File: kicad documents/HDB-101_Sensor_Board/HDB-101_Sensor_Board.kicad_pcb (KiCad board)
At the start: 2 copper layers, 90 x 18 mm, 4 parts, among them J1 Chassis sensor cable

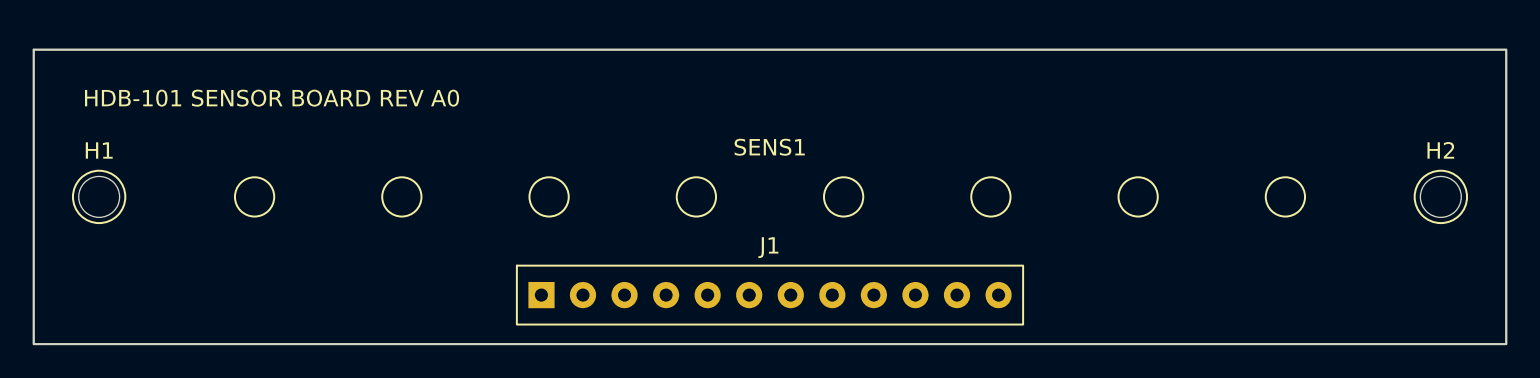
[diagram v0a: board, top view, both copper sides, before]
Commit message: Advance Rev A0 cockpit firmware and PCB bring-up
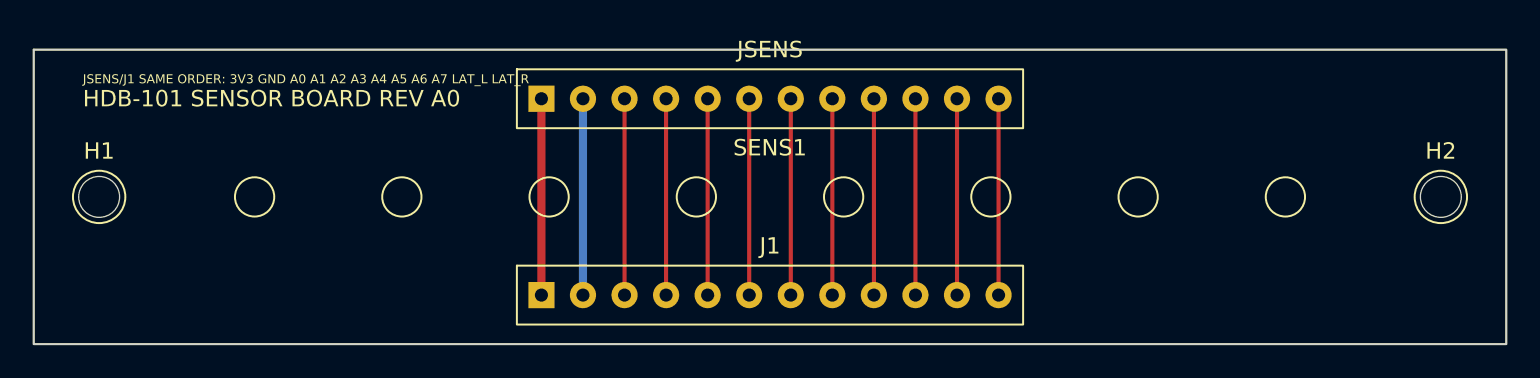
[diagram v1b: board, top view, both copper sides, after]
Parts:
- added JSENS: Sensor module header HPS order, PEGASUS_Placeholders:PinHeader_1x12_2p54, F.Cu at (45.0, 3.00)
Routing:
- net LAT_R: track 0.00 -> 12.0 mm
- net LAT_L: track 0.00 -> 12.0 mm
- net GND: track 0.00 -> 12.0 mm
- net A7: track 0.00 -> 12.0 mm
- net A6: track 0.00 -> 12.0 mm
- net A5: track 0.00 -> 12.0 mm
- net A4: track 0.00 -> 12.0 mm
- net A3: track 0.00 -> 12.0 mm
- net A2: track 0.00 -> 12.0 mm
- net A1: track 0.00 -> 12.0 mm
- net A0: track 0.00 -> 12.0 mm
- net 3V3: track 0.00 -> 12.0 mm
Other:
- board text added: "JSENS/J1 SAME ORDER: 3V3 GND A0 A1 A2 A3 A4 A5 A6 A7 LAT_L LAT_R"
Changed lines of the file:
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@@
     (effects (font (size 0.8 0.8) (thickness 0.15)) (justify left))
+  )
+  (gr_text "JSENS/J1 SAME ORDER: 3V3 GND A0 A1 A2 A3 A4 A5 A6 A7 LAT_L LAT_R" (at 3 1.8) (layer "F.SilkS")
+    (effects (font (size 0.55 0.55) (thickness 0.08)) (justify left))
   )
   (footprint "PEGASUS_Placeholders:SensorAdapter_90x18" (layer "F.Cu")
@@
     (fp_circle (center 22.500 0) (end 23.700 0) (stroke (width 0.12) (type solid)) (fill no) (layer "F.SilkS"))
     (fp_circle (center 31.500 0) (end 32.700 0) (stroke (width 0.12) (type solid)) (fill no) (layer "F.SilkS"))
+  )
+  (footprint "PEGASUS_Placeholders:PinHeader_1x12_2p54" (layer "F.Cu")
+    (at 45.000 3.000 0)
+    (property "Reference" "JSENS" (at 0 -3 0) (layer "F.SilkS")
+      (effects (font (size 1 1) (thickness 0.15)))
+    )
+    (property "Value" "Sensor module header HPS order" (at 0 3 0) (layer "F.Fab")
+      (effects (font (size 1 1) (thickness 0.15)))
+    )
+    (fp_rect (start -15.47 -1.8) (end 15.47 1.8) (stroke (width 0.12) (type solid)) (fill no) (layer "F.SilkS"))
+    (pad "1" thru_hole rect (at -13.970 0.000) (size 1.6 1.6) (drill 0.8) (layers "*.Cu" "*.Mask") (net 1 "3V3"))
+    (pad "2" thru_hole circle (at -11.430 0.000) (size 1.6 1.6) (drill 0.8) (layers "*.Cu" "*.Mask") (net 20 "GND"))
+    (pad "3" thru_hole circle (at -8.890 0.000) (size 1.6 1.6) (drill 0.8) (layers "*.Cu" "*.Mask") (net 3 "A0"))
+    (pad "4" thru_hole circle (at -6.350 0.000) (size 1.6 1.6) (drill 0.8) (layers "*.Cu" "*.Mask") (net 4 "A1"))
+    (pad "5" thru_hole circle (at -3.810 0.000) (size 1.6 1.6) (drill 0.8) (layers "*.Cu" "*.Mask") (net 5 "A2"))
+    (pad "6" thru_hole circle (at -1.270 0.000) (size 1.6 1.6) (drill 0.8) (layers "*.Cu" "*.Mask") (net 6 "A3"))
+    (pad "7" thru_hole circle (at 1.270 0.000) (size 1.6 1.6) (drill 0.8) (layers "*.Cu" "*.Mask") (net 7 "A4"))
+    (pad "8" thru_hole circle (at 3.810 0.000) (size 1.6 1.6) (drill 0.8) (layers "*.Cu" "*.Mask") (net 8 "A5"))
+    (pad "9" thru_hole circle (at 6.350 0.000) (size 1.6 1.6) (drill 0.8) (layers "*.Cu" "*.Mask") (net 9 "A6"))
+    (pad "10" thru_hole circle (at 8.890 0.000) (size 1.6 1.6) (drill 0.8) (layers "*.Cu" "*.Mask") (net 10 "A7"))
+    (pad "11" thru_hole circle (at 11.430 0.000) (size 1.6 1.6) (drill 0.8) (layers "*.Cu" "*.Mask") (net 21 "LAT_L"))
+    (pad "12" thru_hole circle (at 13.970 0.000) (size 1.6 1.6) (drill 0.8) (layers "*.Cu" "*.Mask") (net 22 "LAT_R"))
   )
   (footprint "PEGASUS_Placeholders:PinHeader_1x12_2p54" (layer "F.Cu")
@@
     (pad "" np_thru_hole circle (at 0 0) (size 2.5 2.5) (drill 2.5) (layers "*.Cu" "*.Mask"))
   )
+  (segment (start 31.030 3.000) (end 31.030 15.000) (width 0.50) (layer "F.Cu") (net 1))
+  (segment (start 33.570 3.000) (end 33.570 15.000) (width 0.50) (layer "B.Cu") (net 20))
+  (segment (start 36.110 3.000) (end 36.110 15.000) (width 0.25) (layer "F.Cu") (net 3))
+  (segment (start 38.650 3.000) (end 38.650 15.000) (width 0.25) (layer "F.Cu") (net 4))
+  (segment (start 41.190 3.000) (end 41.190 15.000) (width 0.25) (layer "F.Cu") (net 5))
+  (segment (start 43.730 3.000) (end 43.730 15.000) (width 0.25) (layer "F.Cu") (net 6))
+  (segment (start 46.270 3.000) (end 46.270 15.000) (width 0.25) (layer "F.Cu") (net 7))
+  (segment (start 48.810 3.000) (end 48.810 15.000) (width 0.25) (layer "F.Cu") (net 8))
+  (segment (start 51.350 3.000) (end 51.350 15.000) (width 0.25) (layer "F.Cu") (net 9))
+  (segment (start 53.890 3.000) (end 53.890 15.000) (width 0.25) (layer "F.Cu") (net 10))
+  (segment (start 56.430 3.000) (end 56.430 15.000) (width 0.25) (layer "F.Cu") (net 21))
+  (segment (start 58.970 3.000) (end 58.970 15.000) (width 0.25) (layer "F.Cu") (net 22))
 )
